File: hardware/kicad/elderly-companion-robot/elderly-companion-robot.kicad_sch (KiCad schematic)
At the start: 0 parts

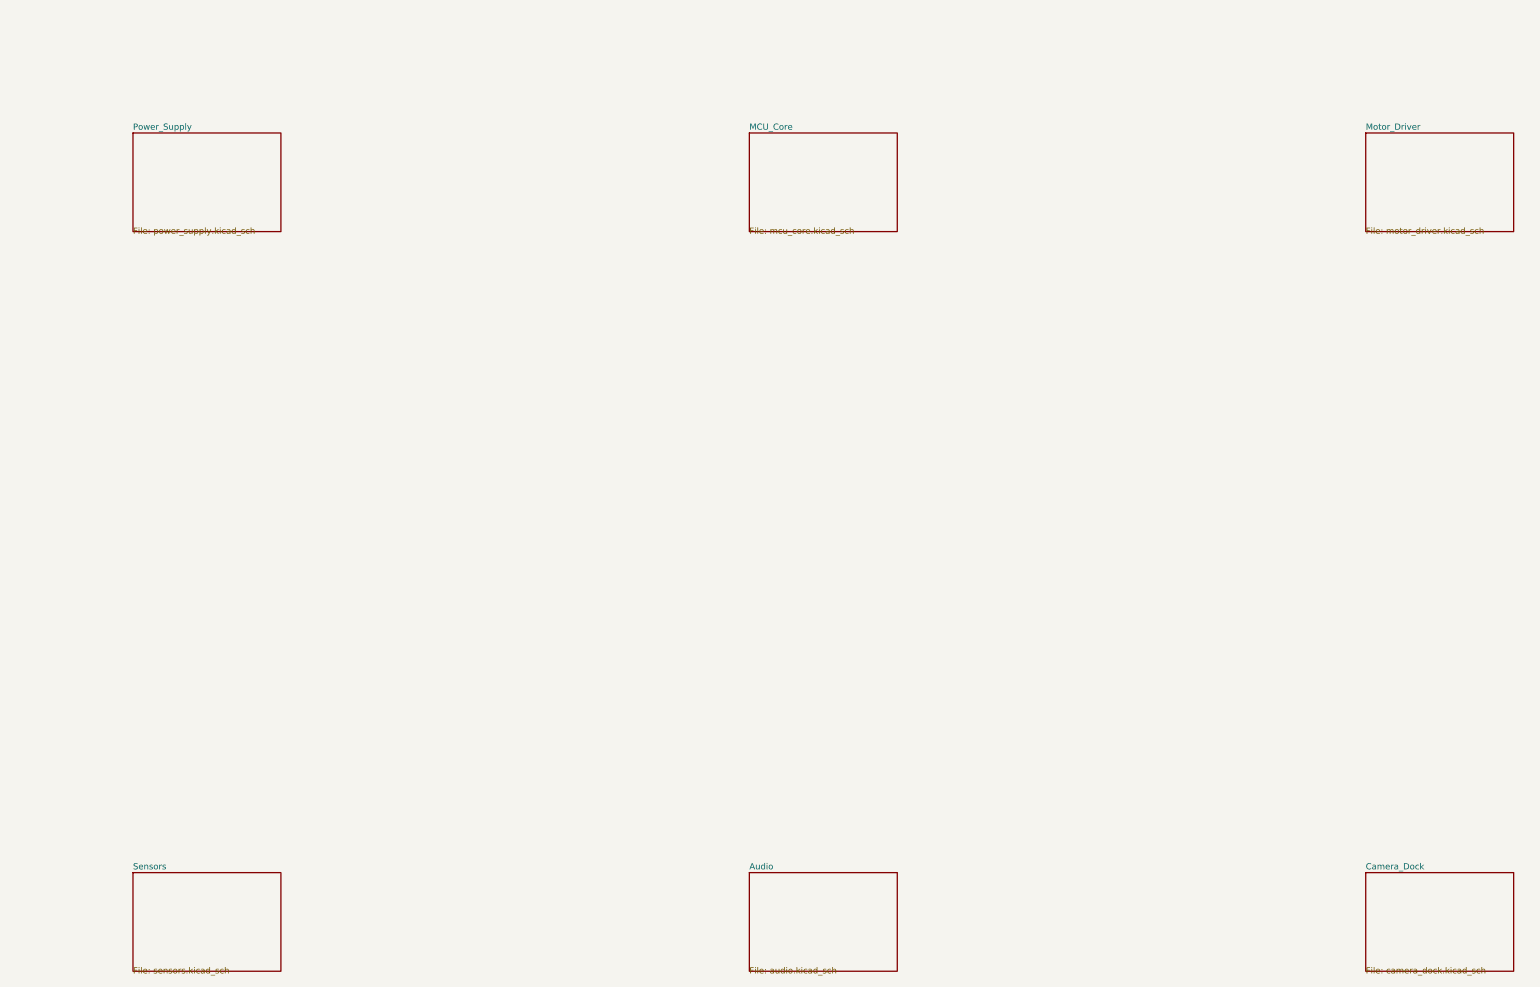
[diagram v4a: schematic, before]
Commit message: Phase 9-10: All 6 hierarchical sheets populated with components, labels, and power symbols
- Power_Supply: LM2596S-5 buck, AP2112K-3.3 LDO, AMS1117-ADJ (4V for SIM800L),
  TP4056 charger, caps, diodes, connectors, resistor dividers
- MCU_Core: ESP32-S3-WROOM-1, 8x decoupling caps, boot/EN resistors,
  hierarchical labels for all peripheral interfaces
- Motor_Driver: L298N, 8x flyback diodes, motor connectors, hierarchical labels
- Sensors: MPU-6050, SSD1306 OLED, 4x HC-SR04 connectors, voltage dividers,
  I2C pull-ups, hierarchical labels
- Audio: MAX98357A, INMP441 connector (6-pin), speaker connector, bypass caps,
  I2S hierarchical labels
- Camera_Dock: SIM800C, 2x servo connectors, IR TX/RX, dock contact,
  UART2/PWRKEY hierarchical labels
- Top-level schematic restored with 6 hierarchical sheet references
- ERC: 0 violations
- Quality gate: Schematic PASS

Co-Authored-By: Claude Opus 4.7 <noreply@anthropic.com>
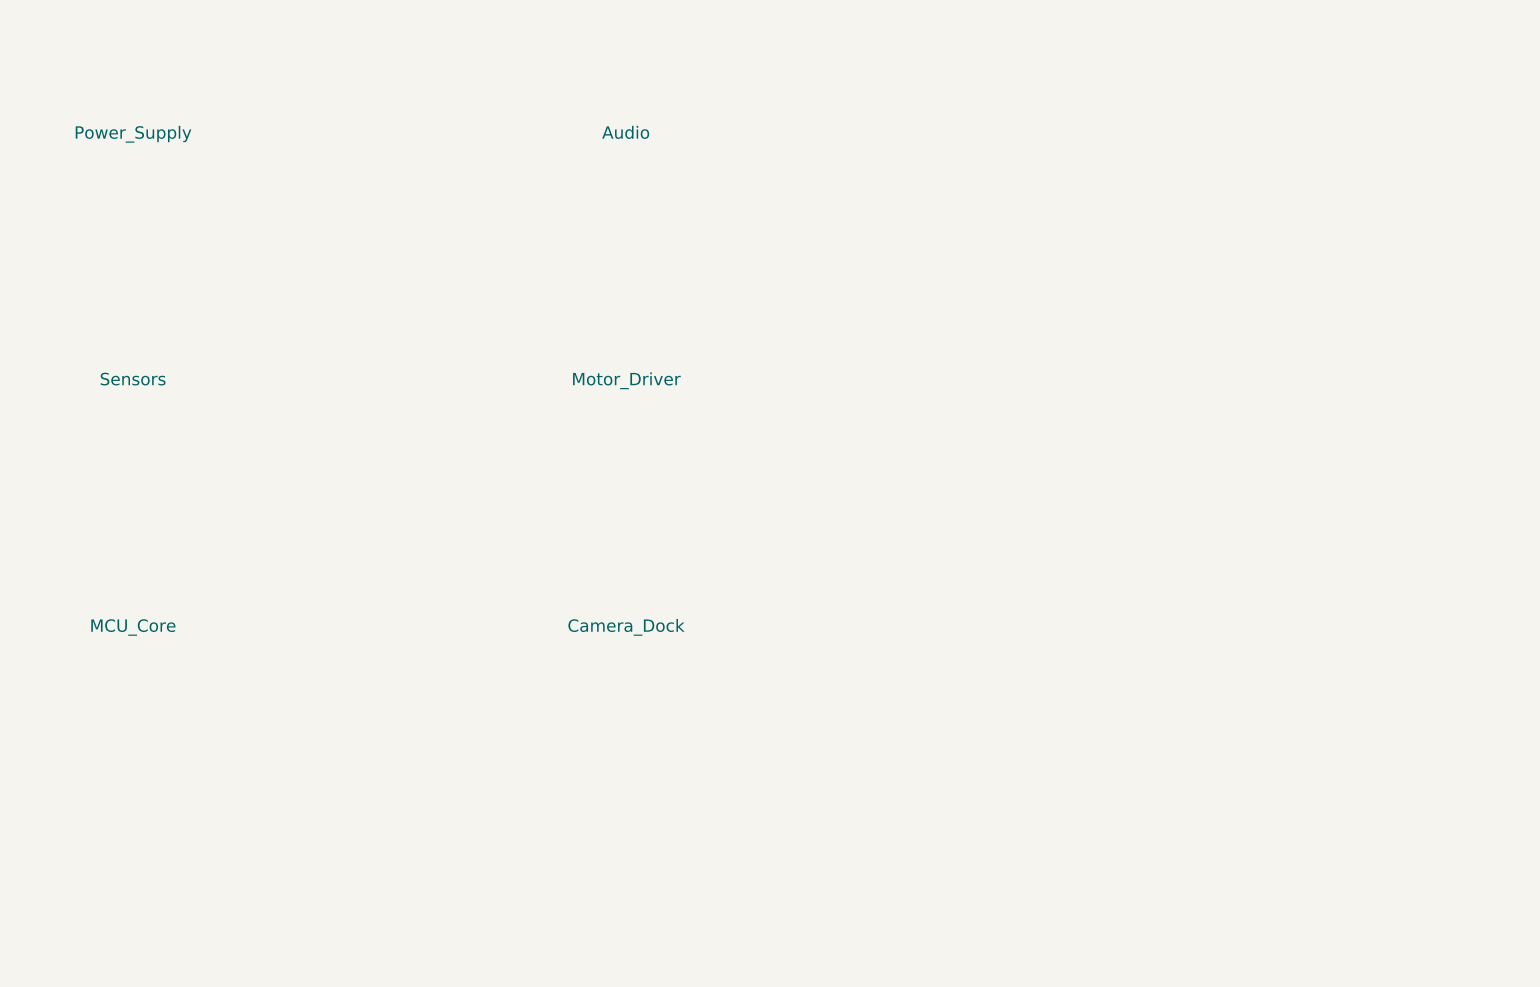
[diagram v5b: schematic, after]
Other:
- sheet Audio: file audio.kicad_sch -> ?
- sheet Camera_Dock: file camera_dock.kicad_sch -> ?
- sheet MCU_Core: file mcu_core.kicad_sch -> ?
- sheet Motor_Driver: file motor_driver.kicad_sch -> ?
- sheet Power_Supply: file power_supply.kicad_sch -> ?
- sheet Sensors: file sensors.kicad_sch -> ?
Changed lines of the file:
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@@
 (kicad_sch
-	(version 20250316)
-	(generator "kicad-mcp-pro")
-	(paper "A4")
+	(version 20250114)
+	(generator "eeschema")
+	(generator_version "9.0")
+	(paper "A3")
 	(title_block
 		(title "Elderly Companion Robot")
-		(date "2025-05-16")
-		(rev "1.0")
+		(date "2025-05-15")
 		(company "yuHz23")
 	)
 	(sheet
-		(at 25.4 25.4)
-		(size 30.48 20.32)
-		(fields_autoplaced yes)
-		(stroke
-			(width 0.1524)
-			(color 0 0 0 1)
-		)
-		(fill
-			(color 0 0 0 0)
-		)
+		(sheetname "Power_Supply")
+		(sheetfile "power_supply.kicad_sch")
 		(property "Sheetname" "Power_Supply"
-			(at 25.4 24.8846 0)
+			(at 25.4 25.4 0)
 			(effects
 				(font
-					(size 1.27 1.27)
+					(size 2.54 2.54)
 				)
-				(justify left bottom)
-			)
-		)
-		(property "Sheetfile" "power_supply.kicad_sch"
-			(at 25.4 46.3296 0)
-			(effects
-				(font
-					(size 1.27 1.27)
-				)
-				(justify left bottom)
 			)
 		)
 	)
 	(sheet
-		(at 152.4 25.4)
-		(size 30.48 20.32)
-		(fields_autoplaced yes)
-		(stroke
-			(width 0.1524)
-			(color 0 0 0 1)
-		)
-		(fill
-			(color 0 0 0 0)
-		)
-		(property "Sheetname" "MCU_Core"
-			(at 152.4 24.8846 0)
+		(sheetname "Sensors")
+		(sheetfile "sensors.kicad_sch")
+		(property "Sheetname" "Sensors"
+			(at 25.4 76.2 0)
 			(effects
 				(font
-					(size 1.27 1.27)
+					(size 2.54 2.54)
 				)
-				(justify left bottom)
-			)
-		)
-		(property "Sheetfile" "mcu_core.kicad_sch"
-			(at 152.4 46.3296 0)
-			(effects
-				(font
-					(size 1.27 1.27)
-				)
-				(justify left bottom)
 			)
 		)
 	)
 	(sheet
-		(at 279.4 25.4)
-		(size 30.48 20.32)
-		(fields_autoplaced yes)
-		(stroke
-			(width 0.1524)
-			(color 0 0 0 1)
-		)
-		(fill
-			(color 0 0 0 0)
-		)
-		(property "Sheetname" "Motor_Driver"
-			(at 279.4 24.8846 0)
+		(sheetname "MCU_Core")
+		(sheetfile "mcu_core.kicad_sch")
+		(property "Sheetname" "MCU_Core"
+			(at 25.4 127 0)
 			(effects
 				(font
-					(size 1.27 1.27)
+					(size 2.54 2.54)
 				)
-				(justify left bottom)
-			)
-		)
-		(property "Sheetfile" "motor_driver.kicad_sch"
-			(at 279.4 46.3296 0)
-			(effects
-				(font
-					(size 1.27 1.27)
-				)
-				(justify left bottom)
 			)
 		)
 	)
 	(sheet
-		(at 25.4 177.8)
-		(size 30.48 20.32)
-		(fields_autoplaced yes)
-		(stroke
-			(width 0.1524)
-			(color 0 0 0 1)
-		)
-		(fill
-			(color 0 0 0 0)
-		)
-		(property "Sheetname" "Sensors"
-			(at 25.4 177.2846 0)
+		(sheetname "Audio")
+		(sheetfile "audio.kicad_sch")
+		(property "Sheetname" "Audio"
+			(at 127 25.4 0)
 			(effects
 				(font
-					(size 1.27 1.27)
+					(size 2.54 2.54)
 				)
-				(justify left bottom)
-			)
-		)
-		(property "Sheetfile" "sensors.kicad_sch"
-			(at 25.4 198.7296 0)
-			(effects
-				(font
-					(size 1.27 1.27)
-				)
-				(justify left bottom)
 			)
 		)
 	)
 	(sheet
-		(at 152.4 177.8)
-		(size 30.48 20.32)
-		(fields_autoplaced yes)
-		(stroke
-			(width 0.1524)
-			(color 0 0 0 1)
-		)
-		(fill
-			(color 0 0 0 0)
-		)
-		(property "Sheetname" "Audio"
-			(at 152.4 177.2846 0)
+		(sheetname "Motor_Driver")
+		(sheetfile "motor_driver.kicad_sch")
+		(property "Sheetname" "Motor_Driver"
+			(at 127 76.2 0)
 			(effects
 				(font
-					(size 1.27 1.27)
+					(size 2.54 2.54)
 				)
-				(justify left bottom)
-			)
-		)
-		(property "Sheetfile" "audio.kicad_sch"
-			(at 152.4 198.7296 0)
-			(effects
-				(font
-					(size 1.27 1.27)
-				)
-				(justify left bottom)
 			)
 		)
 	)
 	(sheet
-		(at 279.4 177.8)
-		(size 30.48 20.32)
-		(fields_autoplaced yes)
-		(stroke
-			(width 0.1524)
-			(color 0 0 0 1)
-		)
-		(fill
-			(color 0 0 0 0)
-		)
+		(sheetname "Camera_Dock")
+		(sheetfile "camera_dock.kicad_sch")
 		(property "Sheetname" "Camera_Dock"
-			(at 279.4 177.2846 0)
+			(at 127 127 0)
 			(effects
 				(font
-					(size 1.27 1.27)
+					(size 2.54 2.54)
 				)
-				(justify left bottom)
-			)
-		)
-		(property "Sheetfile" "camera_dock.kicad_sch"
-			(at 279.4 198.7296 0)
-			(effects
-				(font
-					(size 1.27 1.27)
-				)
-				(justify left bottom)
 			)
 		)
@@
 		)
 	)
+	(embedded_fonts no)
 )
